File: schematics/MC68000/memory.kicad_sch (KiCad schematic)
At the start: 17 parts, among them J1 Conn_02x37_Row_Letter_Last, U13 ROM_LOW, U14 ROM_HIGH, U15 RAM_LOW, U16 RAM_HIGH, U17 GAL20V8, U27 74LS574

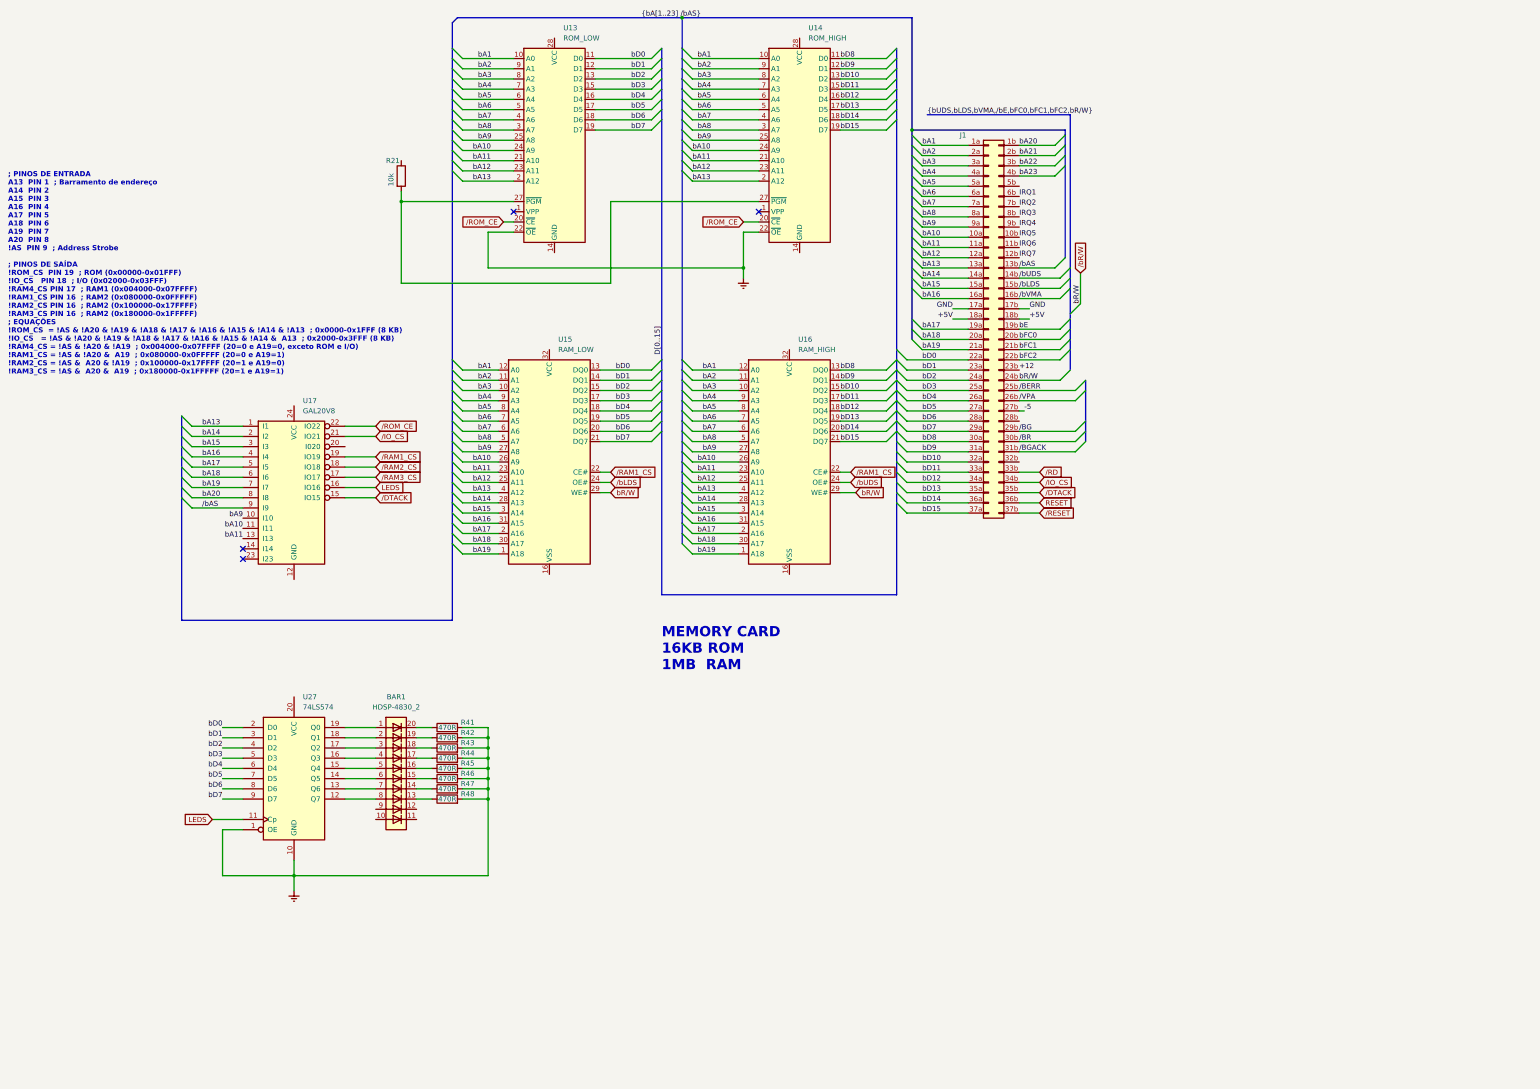
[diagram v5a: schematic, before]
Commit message: Now cpu writes single BYTES to memory...
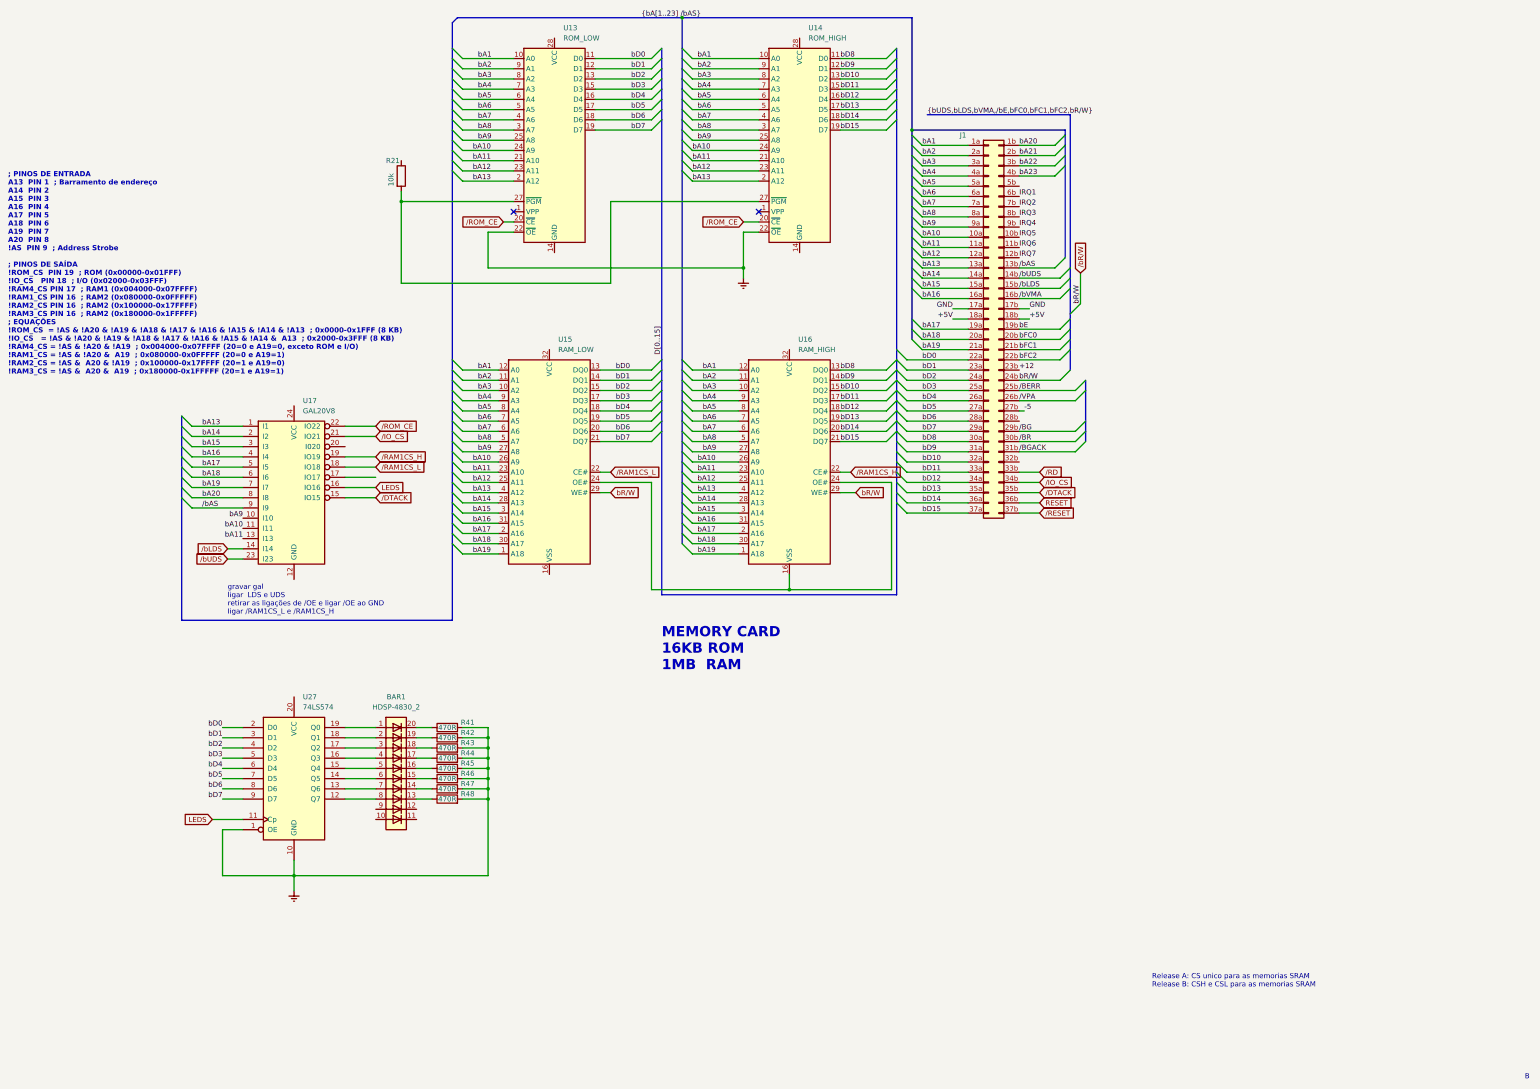
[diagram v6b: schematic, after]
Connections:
- net /bLDS: now also U17.14 (I14); no longer U15.24 (OE#)
- net /bUDS: now also U17.23 (I23); no longer U16.24 (OE#)
- net at U16.16 (VSS): now also U15.24 (OE#), U16.24 (OE#)
- net /RAM1_CS renamed /RAM1CS_H
- net /RAM1CS_H: no longer U15.22 (CE#)
- net /RAM2_CS renamed /RAM1CS_L
- net /RAM1CS_L: now also U15.22 (CE#)
- net /RAM3_CS: no longer names the net of U17.17 (IO17)
- no-connect marks 4 -> 2
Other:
- note added: "B"
- note added: "Release A: CS unico para as memorias SRAM Release B: CSH e CSL para as memorias SRAM"
- note added: "gravar gal ligar LDS e UDS retirar as ligações de /OE e ligar /OE ao GND ligar /RAM1CS_L e /RAM1CS_H"
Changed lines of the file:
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@@
   (junction (at 198.12 78.74) (diameter 0) (color 0 0 0 0)
   )
-  (no_connect (at 73.66 151.13))
+  (junction (at 209.55 158.75) (diameter 0) (color 0 0 0 0)
+  )
   (no_connect (at 201.93 64.77))
-  (no_connect (at 73.66 148.59))
   (no_connect (at 140.97 64.77))
   (bus_entry (at 177.8 116.84) (size -2.54 2.54)
@@
     (stroke (width 0) (type default))
   )
+  (wire (pts (xy 69.85 151.13) (xy 73.66 151.13))
+    (stroke (width 0) (type default))
+  )
   (bus (pts (xy 58.42 133.35) (xy 58.42 135.89))
     (stroke (width 0) (type default))
@@
     (stroke (width 0) (type default))
   )
+  (wire (pts (xy 175.26 132.08) (xy 175.26 158.75))
+    (stroke (width 0) (type default))
+  )
   (wire (pts (xy 161.29 26.67) (xy 175.26 26.67))
     (stroke (width 0) (type default))
@@
     (stroke (width 0) (type default))
   )
+  (wire (pts (xy 175.26 158.75) (xy 209.55 158.75))
+    (stroke (width 0) (type default))
+  )
   (wire (pts (xy 106.68 208.28) (xy 99.06 208.28))
     (stroke (width 0) (type default))
@@
     (stroke (width 0) (type default))
   )
+  (wire (pts (xy 234.95 132.08) (xy 234.95 158.75))
+    (stroke (width 0) (type default))
+  )
   (wire (pts (xy 68.58 218.44) (xy 68.58 229.87))
     (stroke (width 0) (type default))
@@
     (stroke (width 0) (type default))
   )
+  (wire (pts (xy 209.55 158.75) (xy 234.95 158.75))
+    (stroke (width 0) (type default))
+  )
   (bus (pts (xy 240.03 83.82) (xy 240.03 91.44))
     (stroke (width 0) (type default))
@@
     (stroke (width 0) (type default))
   )
-  (wire (pts (xy 222.25 132.08) (xy 224.79 132.08))
+  (wire (pts (xy 222.25 132.08) (xy 234.95 132.08))
     (stroke (width 0) (type default))
   )
@@
     (stroke (width 0) (type default))
   )
+  (wire (pts (xy 209.55 154.94) (xy 209.55 158.75))
+    (stroke (width 0) (type default))
+  )
   (bus (pts (xy 125.73 52.07) (xy 125.73 54.61))
     (stroke (width 0) (type default))
@@
     (stroke (width 0) (type default))
   )
-  (wire (pts (xy 162.56 132.08) (xy 165.1 132.08))
+  (wire (pts (xy 162.56 132.08) (xy 175.26 132.08))
     (stroke (width 0) (type default))
   )
@@
     (stroke (width 0) (type default))
   )
+  (wire (pts (xy 69.85 148.59) (xy 73.66 148.59))
+    (stroke (width 0) (type default))
+  )
   (wire (pts (xy 242.57 66.04) (xy 254 66.04))
     (stroke (width 0) (type default))
@@
   (wire (pts (xy 68.58 210.82) (xy 73.66 210.82))
     (stroke (width 0) (type default))
+  )
+  (text "Release A: CS unico para as memorias SRAM\nRelease B: CSH e CSL para as memorias SRAM\n"
+    (at 299.72 257.81 0)
+    (effects (font (size 1.27 1.27)) (justify left bottom))
   )
   (text "; PINOS DE ENTRADA\nA13  PIN 1  ; Barramento de endereço\nA14  PIN 2\nA15  PIN 3\nA16  PIN 4\nA17  PIN 5\nA18  PIN 6\nA19  PIN 7\nA20  PIN 8\n!AS  PIN 9  ; Address Strobe\n\n; PINOS DE SAÍDA\n!ROM_CS  PIN 19  ; ROM (0x00000-0x01FFF)\n!IO_CS   PIN 18  ; I/O (0x02000-0x03FFF)\n!RAM4_CS PIN 17  ; RAM1 (0x004000-0x07FFFF)\n!RAM1_CS PIN 16  ; RAM2 (0x080000-0x0FFFFF)\n!RAM2_CS PIN 16  ; RAM2 (0x100000-0x17FFFF)\n!RAM3_CS PIN 16  ; RAM2 (0x180000-0x1FFFFF)\n; EQUAÇÕES\n!ROM_CS  = !AS & !A20 & !A19 & !A18 & !A17 & !A16 & !A15 & !A14 & !A13  ; 0x0000-0x1FFF (8 KB)\n!IO_CS   = !AS & !A20 & !A19 & !A18 & !A17 & !A16 & !A15 & !A14 &  A13  ; 0x2000-0x3FFF (8 KB)\n!RAM4_CS = !AS & !A20 & !A19  ; 0x004000-0x07FFFF (20=0 e A19=0, exceto ROM e I/O)\n!RAM1_CS = !AS & !A20 &  A19  ; 0x080000-0x0FFFFF (20=0 e A19=1)\n!RAM2_CS = !AS &  A20 & !A19  ; 0x100000-0x17FFFF (20=1 e A19=0)\n!RAM3_CS = !AS &  A20 &  A19  ; 0x180000-0x1FFFFF (20=1 e A19=1)"
@@
   (text "MEMORY CARD\n16KB ROM\n1MB  RAM" (at 177.8 179.07 0)
     (effects (font (size 2.54 2.54) (thickness 0.508) bold) (justify left bottom))
+  )
+  (text "B" (at 392.43 280.67 0)
+    (effects (font (size 1.27 1.27)) (justify left bottom))
+  )
+  (text "gravar gal\nligar  LDS e UDS\nretirar as ligações de /OE e ligar /OE ao GND\nligar /RAM1CS_L e /RAM1CS_H"
+    (at 69.85 165.1 0)
+    (effects (font (size 1.27 1.27)) (justify left bottom))
   )
   (label "bD10" (at 222.25 31.75 0) (fields_autoplaced)
@@
     )
   )
-  (global_label "{slash}RAM1_CS" (shape input) (at 165.1 129.54 0) (fields_autoplaced)
-    (effects (font (size 1.27 1.27)) (justify left))
-    (property "Intersheetrefs" "${INTERSHEET_REFS}" (at 177.8823 129.54 0)
-      (effects (font (size 1.27 1.27)) (justify left) hide)
-    )
-  )
   (global_label "{slash}IO_CS" (shape input) (at 106.68 120.65 0) (fields_autoplaced)
     (effects (font (size 1.27 1.27)) (justify left))
@@
     )
   )
-  (global_label "{slash}bLDS" (shape input) (at 165.1 132.08 0) (fields_autoplaced)
+  (global_label "{slash}RAM1CS_H" (shape input) (at 224.79 129.54 0) (fields_autoplaced)
     (effects (font (size 1.27 1.27)) (justify left))
-    (property "Intersheetrefs" "${INTERSHEET_REFS}" (at 174.0723 132.08 0)
+    (property "Intersheetrefs" "${INTERSHEET_REFS}" (at 238.9028 129.54 0)
       (effects (font (size 1.27 1.27)) (justify left) hide)
     )
   )
-  (global_label "{slash}RAM3_CS" (shape input) (at 106.68 130.81 0) (fields_autoplaced)
-    (effects (font (size 1.27 1.27)) (justify left))
-    (property "Intersheetrefs" "${INTERSHEET_REFS}" (at 119.4623 130.81 0)
-      (effects (font (size 1.27 1.27)) (justify left) hide)
-    )
-  )
-  (global_label "{slash}RAM1_CS" (shape input) (at 224.79 129.54 0) (fields_autoplaced)
-    (effects (font (size 1.27 1.27)) (justify left))
-    (property "Intersheetrefs" "${INTERSHEET_REFS}" (at 237.5723 129.54 0)
-      (effects (font (size 1.27 1.27)) (justify left) hide)
-    )
-  )
-  (global_label "{slash}bUDS" (shape input) (at 224.79 132.08 0) (fields_autoplaced)
-    (effects (font (size 1.27 1.27)) (justify left))
-    (property "Intersheetrefs" "${INTERSHEET_REFS}" (at 234.0647 132.08 0)
-      (effects (font (size 1.27 1.27)) (justify left) hide)
+  (global_label "{slash}bLDS" (shape input) (at 69.85 148.59 180) (fields_autoplaced)
+    (effects (font (size 1.27 1.27)) (justify right))
+    (property "Intersheetrefs" "${INTERSHEET_REFS}" (at 60.8777 148.59 0)
+      (effects (font (size 1.27 1.27)) (justify right) hide)
     )
   )
@@
     )
   )
-  (global_label "{slash}RAM2_CS" (shape input) (at 106.68 128.27 0) (fields_autoplaced)
-    (effects (font (size 1.27 1.27)) (justify left))
-    (property "Intersheetrefs" "${INTERSHEET_REFS}" (at 119.4623 128.27 0)
-      (effects (font (size 1.27 1.27)) (justify left) hide)
-    )
-  )
   (global_label "{slash}ROM_CE" (shape input) (at 106.68 118.11 0) (fields_autoplaced)
     (effects (font (size 1.27 1.27)) (justify left))
@@
     )
   )
-  (global_label "{slash}RAM1_CS" (shape input) (at 106.68 125.73 0) (fields_autoplaced)
+  (global_label "{slash}RAM1CS_H" (shape input) (at 106.68 125.73 0) (fields_autoplaced)
     (effects (font (size 1.27 1.27)) (justify left))
-    (property "Intersheetrefs" "${INTERSHEET_REFS}" (at 119.4623 125.73 0)
+    (property "Intersheetrefs" "${INTERSHEET_REFS}" (at 120.7928 125.73 0)
+      (effects (font (size 1.27 1.27)) (justify left) hide)
+    )
+  )
+  (global_label "{slash}RAM1CS_L" (shape input) (at 106.68 128.27 0) (fields_autoplaced)
+    (effects (font (size 1.27 1.27)) (justify left))
+    (property "Intersheetrefs" "${INTERSHEET_REFS}" (at 120.4904 128.27 0)
       (effects (font (size 1.27 1.27)) (justify left) hide)
     )
@@
     )
   )
+  (global_label "{slash}bUDS" (shape input) (at 69.85 151.13 180) (fields_autoplaced)
+    (effects (font (size 1.27 1.27)) (justify right))
+    (property "Intersheetrefs" "${INTERSHEET_REFS}" (at 60.5753 151.13 0)
+      (effects (font (size 1.27 1.27)) (justify right) hide)
+    )
+  )
   (global_label "{slash}RD" (shape input) (at 271.78 129.54 0) (fields_autoplaced)
     (effects (font (size 1.27 1.27)) (justify left))
@@
       (effects (font (size 1.27 1.27)) (justify left) hide)
     )
+  )
+  (global_label "{slash}RAM1CS_L" (shape input) (at 165.1 129.54 0) (fields_autoplaced)
+    (effects (font (size 1.27 1.27)) (justify left))
+    (property "Intersheetrefs" "${INTERSHEET_REFS}" (at 178.9104 129.54 0)
+      (effects (font (size 1.27 1.27)) (justify left) hide)
+    )

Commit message: Update 2025/08/14 17:00
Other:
- note removed: "; PINOS DE ENTRADA A13 PIN 1 ; Barramento de endereço A14 PIN 2 A15 PIN 3 A16 PIN 4 A17 PIN 5 A18 PIN 6 A19 PIN 7 A20 PIN 8 !AS PIN 9 ; Address Strobe ; PINOS DE SAÍDA !ROM_CS PIN 19 ; ROM (0x00000-0x01FFF) !IO_CS PIN 18 ; I/O (0x02000-0x03FFF) !RAM4_CS PIN 17 ; RAM1 (0x004000-0x07FFFF) !RAM1_CS PIN 16 ; RAM2 (0x080000-0x0FFFFF) !RAM2_CS PIN 16 ; RAM2 (0x100000-0x17FFFF) !RAM3_CS PIN 16 ; RAM2 (0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"
- note removed: "gravar gal ligar LDS e UDS retirar as ligações de /OE e ligar /OE ao GND ligar /RAM1CS_L e /RAM1CS_H"
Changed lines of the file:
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@@
     (effects (font (size 1.27 1.27)) (justify left bottom))
-  )
-  (text "; PINOS DE ENTRADA\nA13  PIN 1  ; Barramento de endereço\nA14  PIN 2\nA15  PIN 3\nA16  PIN 4\nA17  PIN 5\nA18  PIN 6\nA19  PIN 7\nA20  PIN 8\n!AS  PIN 9  ; Address Strobe\n\n; PINOS DE SAÍDA\n!ROM_CS  PIN 19  ; ROM (0x00000-0x01FFF)\n!IO_CS   PIN 18  ; I/O (0x02000-0x03FFF)\n!RAM4_CS PIN 17  ; RAM1 (0x004000-0x07FFFF)\n!RAM1_CS PIN 16  ; RAM2 (0x080000-0x0FFFFF)\n!RAM2_CS PIN 16  ; RAM2 (0x100000-0x17FFFF)\n!RAM3_CS PIN 16  ; RAM2 (0x180000-0x1FFFFF)\n; EQUAÇÕES\n!ROM_CS  = !AS & !A20 & !A19 & !A18 & !A17 & !A16 & !A15 & !A14 & !A13  ; 0x0000-0x1FFF (8 KB)\n!IO_CS   = !AS & !A20 & !A19 & !A18 & !A17 & !A16 & !A15 & !A14 &  A13  ; 0x2000-0x3FFF (8 KB)\n!RAM4_CS = !AS & !A20 & !A19  ; 0x004000-0x07FFFF (20=0 e A19=0, exceto ROM e I/O)\n!RAM1_CS = !AS & !A20 &  A19  ; 0x080000-0x0FFFFF (20=0 e A19=1)\n!RAM2_CS = !AS &  A20 & !A19  ; 0x100000-0x17FFFF (20=1 e A19=0)\n!RAM3_CS = !AS &  A20 &  A19  ; 0x180000-0x1FFFFF (20=1 e A19=1)"
-    (at 15.24 105.41 0)
-    (effects (font (size 1.27 1.27) (thickness 0.254) bold) (justify left bottom))
   )
   (text "MEMORY CARD\n16KB ROM\n1MB  RAM" (at 177.8 179.07 0)
@@
     (effects (font (size 1.27 1.27)) (justify left bottom))
   )
-  (text "gravar gal\nligar  LDS e UDS\nretirar as ligações de /OE e ligar /OE ao GND\nligar /RAM1CS_L e /RAM1CS_H"
-    (at 69.85 165.1 0)
-    (effects (font (size 1.27 1.27)) (justify left bottom))
-  )

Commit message: update...
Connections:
- net bE: no longer names the net of J1.19b (Pin_19b)
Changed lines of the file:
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@@
-    (stroke (width 0) (type default))
-  )
-  (bus_entry (at 279.4 91.44) (size -2.54 2.54)
     (stroke (width 0) (type default))
   )
@@
   )
   (bus (pts (xy 125.73 137.16) (xy 125.73 139.7))
-    (stroke (width 0) (type default))
-  )
-  (wire (pts (xy 276.86 93.98) (xy 266.7 93.98))
     (stroke (width 0) (type default))
   )
@@
     (effects (font (size 1.27 1.27)) (justify left bottom))
   )
-  (label "bE" (at 266.7 93.98 0) (fields_autoplaced)
-    (effects (font (size 1.27 1.27)) (justify left bottom))
-  )
